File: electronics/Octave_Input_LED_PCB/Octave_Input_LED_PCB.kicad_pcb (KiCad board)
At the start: 2 copper layers, 76.2 x 57.2 mm, 37 parts, among them J3 Conn_01x12, SW1 SW_Hot_Swap_Socket, SW10 SW_Hot_Swap_Socket, SW11 SW_Hot_Swap_Socket, SW12 SW_Hot_Swap_Socket, SW2 SW_Hot_Swap_Socket, SW3 SW_Hot_Swap_Socket, SW4 SW_Hot_Swap_Socket, SW5 SW_Hot_Swap_Socket, SW6 SW_Hot_Swap_Socket, SW7 SW_Hot_Swap_Socket, SW8 SW_Hot_Swap_Socket, SW9 SW_Hot_Swap_Socket

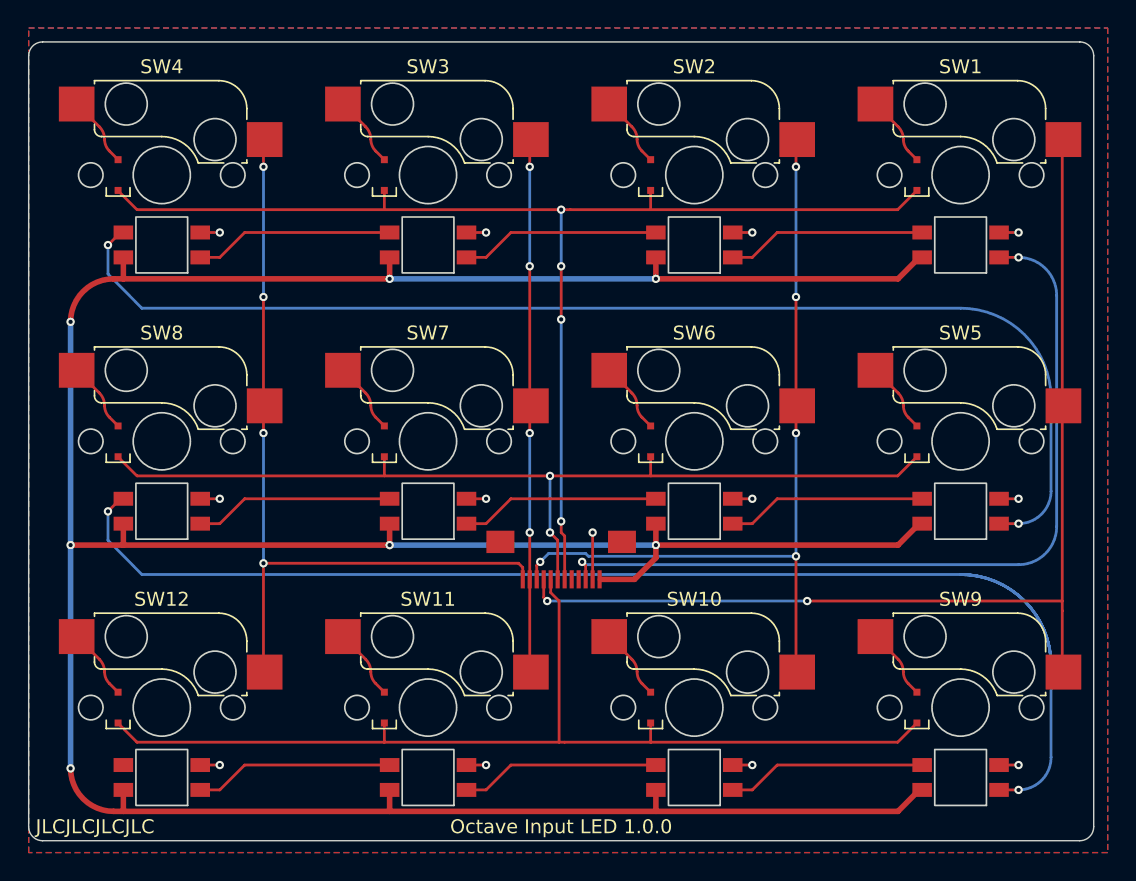
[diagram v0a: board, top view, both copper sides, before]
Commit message: Improve footprint of WS2812B-Mini_Inverted
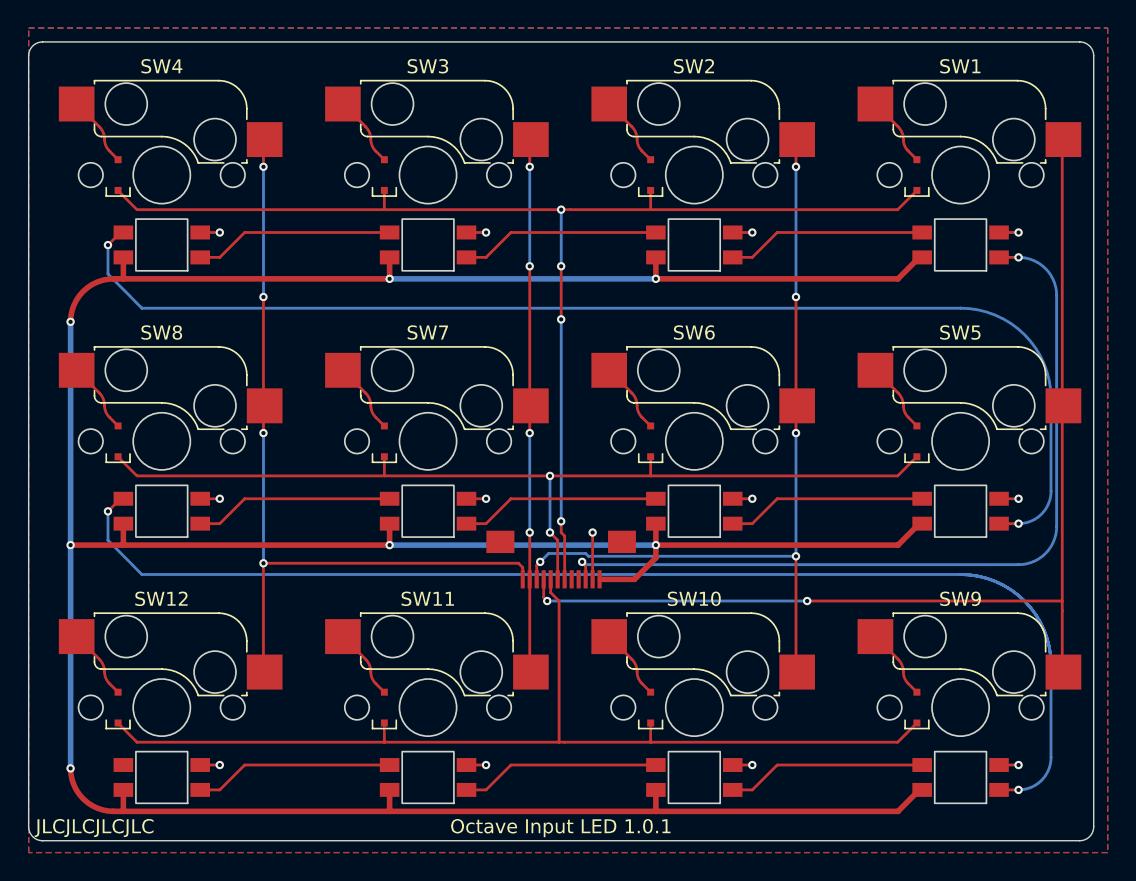
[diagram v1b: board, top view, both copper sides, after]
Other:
- board text added: "Octave Input LED 1.0.1"
- board text removed: "Octave Input LED 1.0.0"
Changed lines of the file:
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@@
   (title_block
     (title "Octave - Input LED PCB")
-    (date "2023-03-21")
-    (rev "1.0.0")
+    (date "2023-04-09")
+    (rev "1.0.1")
     (comment 4 "https://github.com/takayoshiotake/octave-12-key-macropad")
   )
@@
       (effects (font (size 0.5 0.5) (thickness 0.1)))
     )
-    (fp_rect (start -1.85 -2) (end 1.85 2) (layer "Edge.Cuts") (width 0.12) (fill none))
-    (fp_rect (start -3.65 -2.2) (end 3.65 2.2) (layer "F.CrtYd") (width 0.05) (fill none))
+    (fp_rect (start -1.85 -1.85) (end 1.85 1.85) (layer "Edge.Cuts") (width 0.12) (fill none))
+    (fp_rect (start -3.65 -2.05) (end 3.65 2.05) (layer "F.CrtYd") (width 0.05) (fill none))
     (fp_rect (start -1.74 -1.74) (end 1.74 1.74) (layer "F.Fab") (width 0.1) (fill none))
     (fp_circle (center -1.45 1.45) (end -1.25 1.45) (layer "F.Fab") (width 0.1) (fill none))
@@
       (effects (font (size 0.5 0.5) (thickness 0.1)))
     )
-    (fp_rect (start -1.85 -2) (end 1.85 2) (layer "Edge.Cuts") (width 0.12) (fill none))
-    (fp_rect (start -3.65 -2.2) (end 3.65 2.2) (layer "F.CrtYd") (width 0.05) (fill none))
+    (fp_rect (start -1.85 -1.85) (end 1.85 1.85) (layer "Edge.Cuts") (width 0.12) (fill none))
+    (fp_rect (start -3.65 -2.05) (end 3.65 2.05) (layer "F.CrtYd") (width 0.05) (fill none))
     (fp_rect (start -1.74 -1.74) (end 1.74 1.74) (layer "F.Fab") (width 0.1) (fill none))
     (fp_circle (center -1.45 1.45) (end -1.25 1.45) (layer "F.Fab") (width 0.1) (fill none))
@@
       (effects (font (size 0.5 0.5) (thickness 0.1)))
     )
-    (fp_rect (start -1.85 -2) (end 1.85 2) (layer "Edge.Cuts") (width 0.12) (fill none))
-    (fp_rect (start -3.65 -2.2) (end 3.65 2.2) (layer "F.CrtYd") (width 0.05) (fill none))
+    (fp_rect (start -1.85 -1.85) (end 1.85 1.85) (layer "Edge.Cuts") (width 0.12) (fill none))
+    (fp_rect (start -3.65 -2.05) (end 3.65 2.05) (layer "F.CrtYd") (width 0.05) (fill none))
     (fp_rect (start -1.74 -1.74) (end 1.74 1.74) (layer "F.Fab") (width 0.1) (fill none))
     (fp_circle (center -1.45 1.45) (end -1.25 1.45) (layer "F.Fab") (width 0.1) (fill none))
@@
       (effects (font (size 0.5 0.5) (thickness 0.1)))
     )
-    (fp_rect (start -1.85 -2) (end 1.85 2) (layer "Edge.Cuts") (width 0.12) (fill none))
-    (fp_rect (start -3.65 -2.2) (end 3.65 2.2) (layer "F.CrtYd") (width 0.05) (fill none))
+    (fp_rect (start -1.85 -1.85) (end 1.85 1.85) (layer "Edge.Cuts") (width 0.12) (fill none))
+    (fp_rect (start -3.65 -2.05) (end 3.65 2.05) (layer "F.CrtYd") (width 0.05) (fill none))
     (fp_rect (start -1.74 -1.74) (end 1.74 1.74) (layer "F.Fab") (width 0.1) (fill none))
     (fp_circle (center -1.45 1.45) (end -1.25 1.45) (layer "F.Fab") (width 0.1) (fill none))
@@
       (effects (font (size 0.5 0.5) (thickness 0.1)))
     )
-    (fp_rect (start -1.85 -2) (end 1.85 2) (layer "Edge.Cuts") (width 0.12) (fill none))
-    (fp_rect (start -3.65 -2.2) (end 3.65 2.2) (layer "F.CrtYd") (width 0.05) (fill none))
+    (fp_rect (start -1.85 -1.85) (end 1.85 1.85) (layer "Edge.Cuts") (width 0.12) (fill none))
+    (fp_rect (start -3.65 -2.05) (end 3.65 2.05) (layer "F.CrtYd") (width 0.05) (fill none))
     (fp_rect (start -1.74 -1.74) (end 1.74 1.74) (layer "F.Fab") (width 0.1) (fill none))
     (fp_circle (center -1.45 1.45) (end -1.25 1.45) (layer "F.Fab") (width 0.1) (fill none))
@@
       (effects (font (size 0.5 0.5) (thickness 0.1)))
     )
-    (fp_rect (start -1.85 -2) (end 1.85 2) (layer "Edge.Cuts") (width 0.12) (fill none))
-    (fp_rect (start -3.65 -2.2) (end 3.65 2.2) (layer "F.CrtYd") (width 0.05) (fill none))
+    (fp_rect (start -1.85 -1.85) (end 1.85 1.85) (layer "Edge.Cuts") (width 0.12) (fill none))
+    (fp_rect (start -3.65 -2.05) (end 3.65 2.05) (layer "F.CrtYd") (width 0.05) (fill none))
     (fp_rect (start -1.74 -1.74) (end 1.74 1.74) (layer "F.Fab") (width 0.1) (fill none))
     (fp_circle (center -1.45 1.45) (end -1.25 1.45) (layer "F.Fab") (width 0.1) (fill none))
@@
       (effects (font (size 0.5 0.5) (thickness 0.1)))
     )
-    (fp_rect (start -1.85 -2) (end 1.85 2) (layer "Edge.Cuts") (width 0.12) (fill none))
-    (fp_rect (start -3.65 -2.2) (end 3.65 2.2) (layer "F.CrtYd") (width 0.05) (fill none))
+    (fp_rect (start -1.85 -1.85) (end 1.85 1.85) (layer "Edge.Cuts") (width 0.12) (fill none))
+    (fp_rect (start -3.65 -2.05) (end 3.65 2.05) (layer "F.CrtYd") (width 0.05) (fill none))
     (fp_rect (start -1.74 -1.74) (end 1.74 1.74) (layer "F.Fab") (width 0.1) (fill none))
     (fp_circle (center -1.45 1.45) (end -1.25 1.45) (layer "F.Fab") (width 0.1) (fill none))
@@
       (effects (font (size 0.5 0.5) (thickness 0.1)))
     )
-    (fp_rect (start -1.85 -2) (end 1.85 2) (layer "Edge.Cuts") (width 0.12) (fill none))
-    (fp_rect (start -3.65 -2.2) (end 3.65 2.2) (layer "F.CrtYd") (width 0.05) (fill none))
+    (fp_rect (start -1.85 -1.85) (end 1.85 1.85) (layer "Edge.Cuts") (width 0.12) (fill none))
+    (fp_rect (start -3.65 -2.05) (end 3.65 2.05) (layer "F.CrtYd") (width 0.05) (fill none))
     (fp_rect (start -1.74 -1.74) (end 1.74 1.74) (layer "F.Fab") (width 0.1) (fill none))
     (fp_circle (center -1.45 1.45) (end -1.25 1.45) (layer "F.Fab") (width 0.1) (fill none))
@@
       (effects (font (size 0.5 0.5) (thickness 0.1)))
     )
-    (fp_rect (start -1.85 -2) (end 1.85 2) (layer "Edge.Cuts") (width 0.12) (fill none))
-    (fp_rect (start -3.65 -2.2) (end 3.65 2.2) (layer "F.CrtYd") (width 0.05) (fill none))
+    (fp_rect (start -1.85 -1.85) (end 1.85 1.85) (layer "Edge.Cuts") (width 0.12) (fill none))
+    (fp_rect (start -3.65 -2.05) (end 3.65 2.05) (layer "F.CrtYd") (width 0.05) (fill none))
     (fp_rect (start -1.74 -1.74) (end 1.74 1.74) (layer "F.Fab") (width 0.1) (fill none))
     (fp_circle (center -1.45 1.45) (end -1.25 1.45) (layer "F.Fab") (width 0.1) (fill none))
@@
       (effects (font (size 0.5 0.5) (thickness 0.1)))
     )
-    (fp_rect (start -1.85 -2) (end 1.85 2) (layer "Edge.Cuts") (width 0.12) (fill none))
-    (fp_rect (start -3.65 -2.2) (end 3.65 2.2) (layer "F.CrtYd") (width 0.05) (fill none))
+    (fp_rect (start -1.85 -1.85) (end 1.85 1.85) (layer "Edge.Cuts") (width 0.12) (fill none))
+    (fp_rect (start -3.65 -2.05) (end 3.65 2.05) (layer "F.CrtYd") (width 0.05) (fill none))
     (fp_rect (start -1.74 -1.74) (end 1.74 1.74) (layer "F.Fab") (width 0.1) (fill none))
     (fp_circle (center -1.45 1.45) (end -1.25 1.45) (layer "F.Fab") (width 0.1) (fill none))
@@
       (effects (font (size 0.5 0.5) (thickness 0.1)))
     )
-    (fp_rect (start -1.85 -2) (end 1.85 2) (layer "Edge.Cuts") (width 0.12) (fill none))
-    (fp_rect (start -3.65 -2.2) (end 3.65 2.2) (layer "F.CrtYd") (width 0.05) (fill none))
+    (fp_rect (start -1.85 -1.85) (end 1.85 1.85) (layer "Edge.Cuts") (width 0.12) (fill none))
+    (fp_rect (start -3.65 -2.05) (end 3.65 2.05) (layer "F.CrtYd") (width 0.05) (fill none))
     (fp_rect (start -1.74 -1.74) (end 1.74 1.74) (layer "F.Fab") (width 0.1) (fill none))
     (fp_circle (center -1.45 1.45) (end -1.25 1.45) (layer "F.Fab") (width 0.1) (fill none))
@@
       (effects (font (size 0.5 0.5) (thickness 0.1)))
     )
-    (fp_rect (start -1.85 -2) (end 1.85 2) (layer "Edge.Cuts") (width 0.12) (fill none))
-    (fp_rect (start -3.65 -2.2) (end 3.65 2.2) (layer "F.CrtYd") (width 0.05) (fill none))
+    (fp_rect (start -1.85 -1.85) (end 1.85 1.85) (layer "Edge.Cuts") (width 0.12) (fill none))
+    (fp_rect (start -3.65 -2.05) (end 3.65 2.05) (layer "F.CrtYd") (width 0.05) (fill none))
     (fp_rect (start -1.74 -1.74) (end 1.74 1.74) (layer "F.Fab") (width 0.1) (fill none))
     (fp_circle (center -1.45 1.45) (end -1.25 1.45) (layer "F.Fab") (width 0.1) (fill none))
@@
     (effects (font (size 1 1) (thickness 0.15)) (justify left))
   )
-  (gr_text "Octave Input LED 1.0.0" (at 105.1 87.15) (layer "F.SilkS")
+  (gr_text "Octave Input LED 1.0.1" (at 105.1 87.15) (layer "F.SilkS")
     (effects (font (size 1 1) (thickness 0.15)))
   )
